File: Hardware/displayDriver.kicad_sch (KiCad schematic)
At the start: 21 parts, among them J3 Conn_01x10, J4 Conn_01x10, Q1 BSS138, U10 4511, U11 HDSP-816E, U13 HDSP-816E, U6 4511, U7 HDSP-816E, U8 4511, U9 HDSP-816E

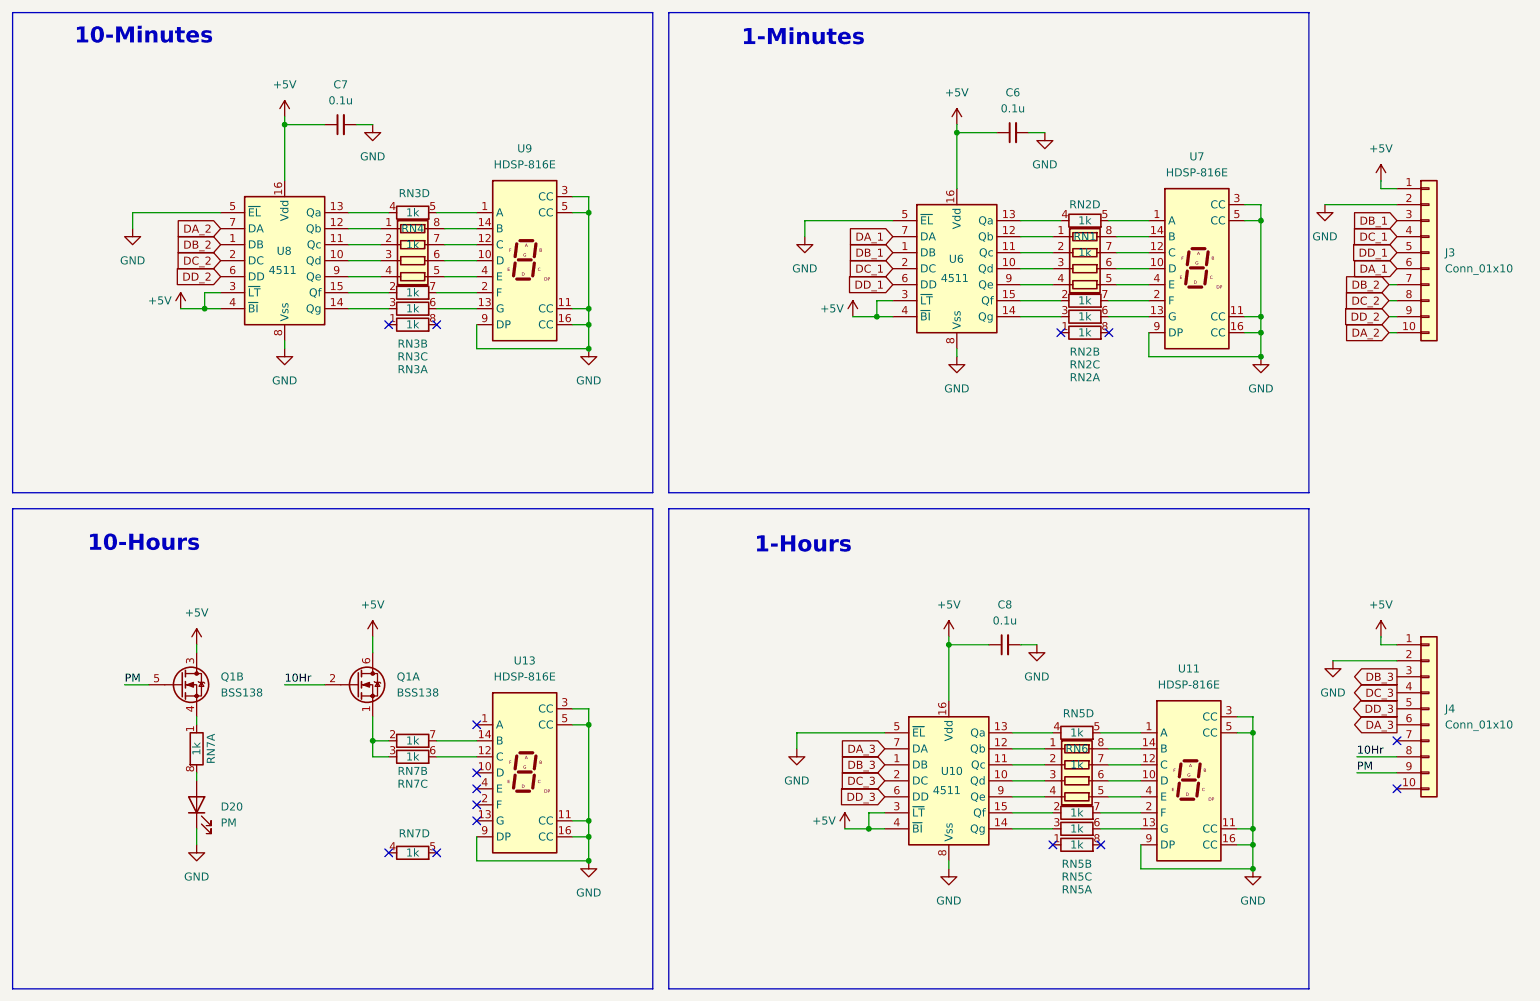
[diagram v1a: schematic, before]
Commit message: chore: update to actual displays
Change generic displays to actual implemented displays. Includes new symbol library for the retro HP 5082 parts.

Also update the power supply to use 7805 (due to thermals).
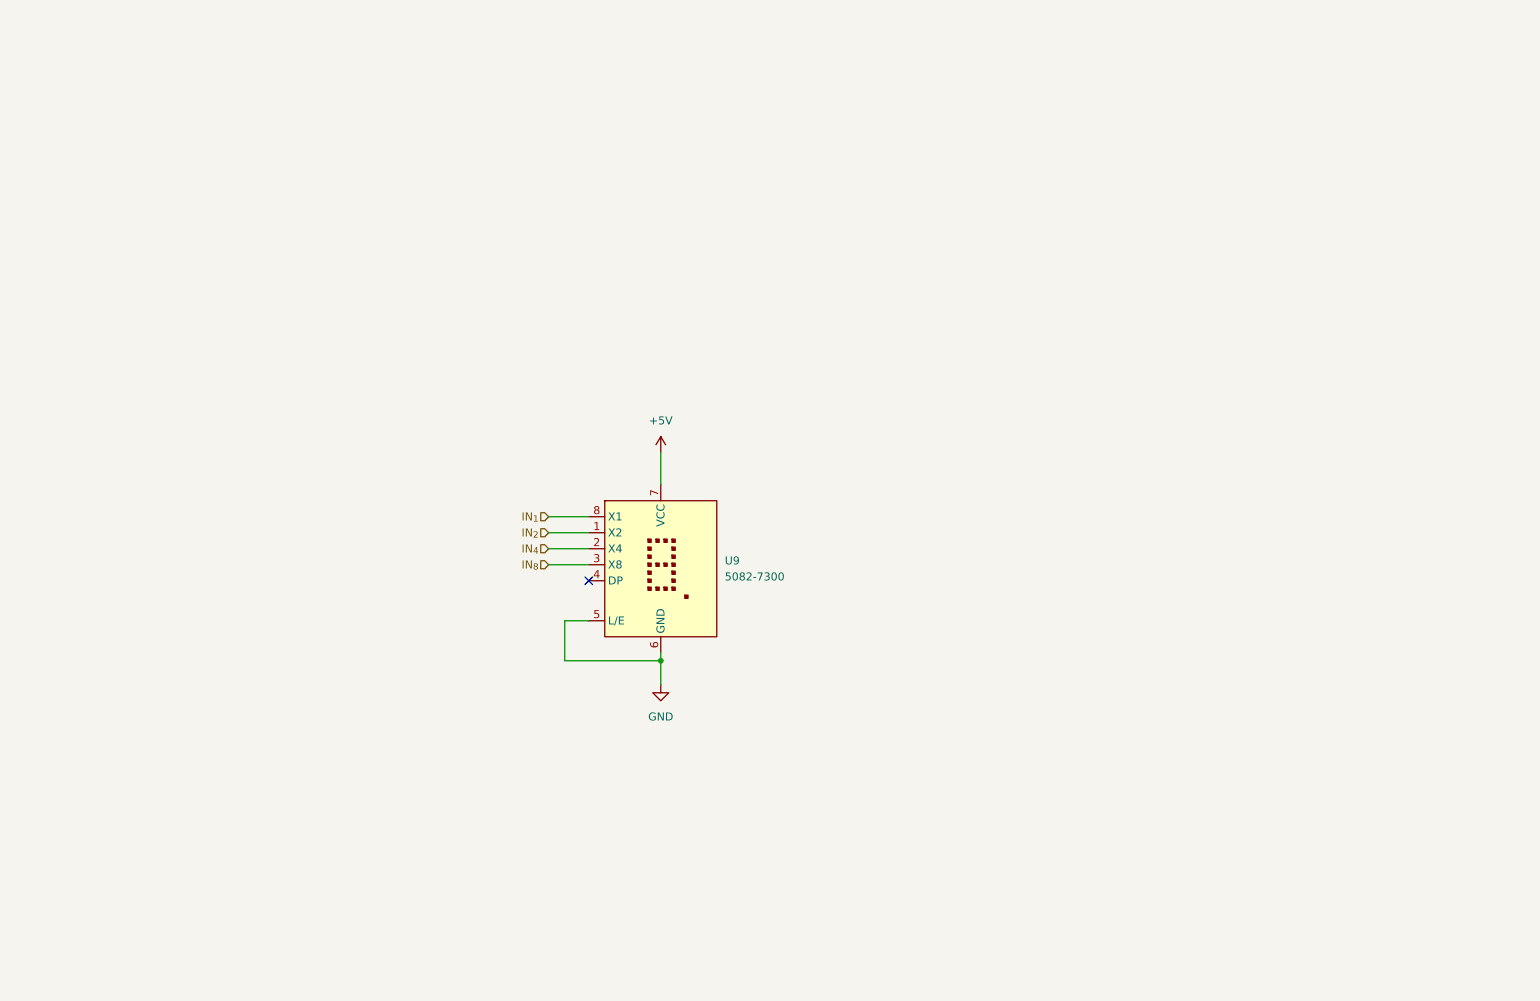
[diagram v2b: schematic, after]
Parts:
- removed C6, C7, C8: 0.1u, Capacitor_SMD:C_0603_1608Metric, symbol Device:C_Small
- removed D20: PM, LED_THT:LED_D5.0mm, symbol Device:LED
- removed J3, J4: Conn_01x10, Connector_PinSocket_2.54mm:PinSocket_1x10_P2.54mm_Vertical, symbol Connector_Generic:Conn_01x10
- removed Q1: BSS138, Package_TO_SOT_SMD:SOT-363_SC-70-6, symbol JKC_library:BSS138_dual
- removed RN1, RN4, RN6: 1k, Resistor_SMD:R_Array_Convex_4x0603, symbol Device:R_Pack04
- removed RN2, RN3, RN5, RN7: 1k, Resistor_SMD:R_Array_Convex_4x0603, symbol Device:R_Pack04_Split
- removed U10, U6, U8: 4511, Package_SO:TSSOP-16_4.4x5mm_P0.65mm, symbol 4xxx_IEEE:4511
- removed U11, U13, U7, U9: HDSP-816E, JKC_Library:Broadcom_HDSP-81x, symbol JKC_library:HDSP-816E
- added U9: 5082-7300, symbol retro_parts:5082-7300
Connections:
- net +5V: now also U9.7 (VCC)
- net GND: now also U9.5 (L/E), U9.6 (GND)
- new net IN_{1}: U9.8 (X1)
- new net IN_{2}: U9.1 (X2)
- new net IN_{4}: U9.2 (X4)
- new net IN_{8}: U9.3 (X8)
- no-connect marks 15 -> 1
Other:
- note removed: "1-Hours"
- note removed: "1-Minutes"
- note removed: "10-Hours"
- note removed: "10-Minutes"
- title: (none) -> AC Clock
